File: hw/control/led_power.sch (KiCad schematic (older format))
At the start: 19 parts, among them Q1001 BC807, Q1002 BC817, U801 LM2678T-ADJ

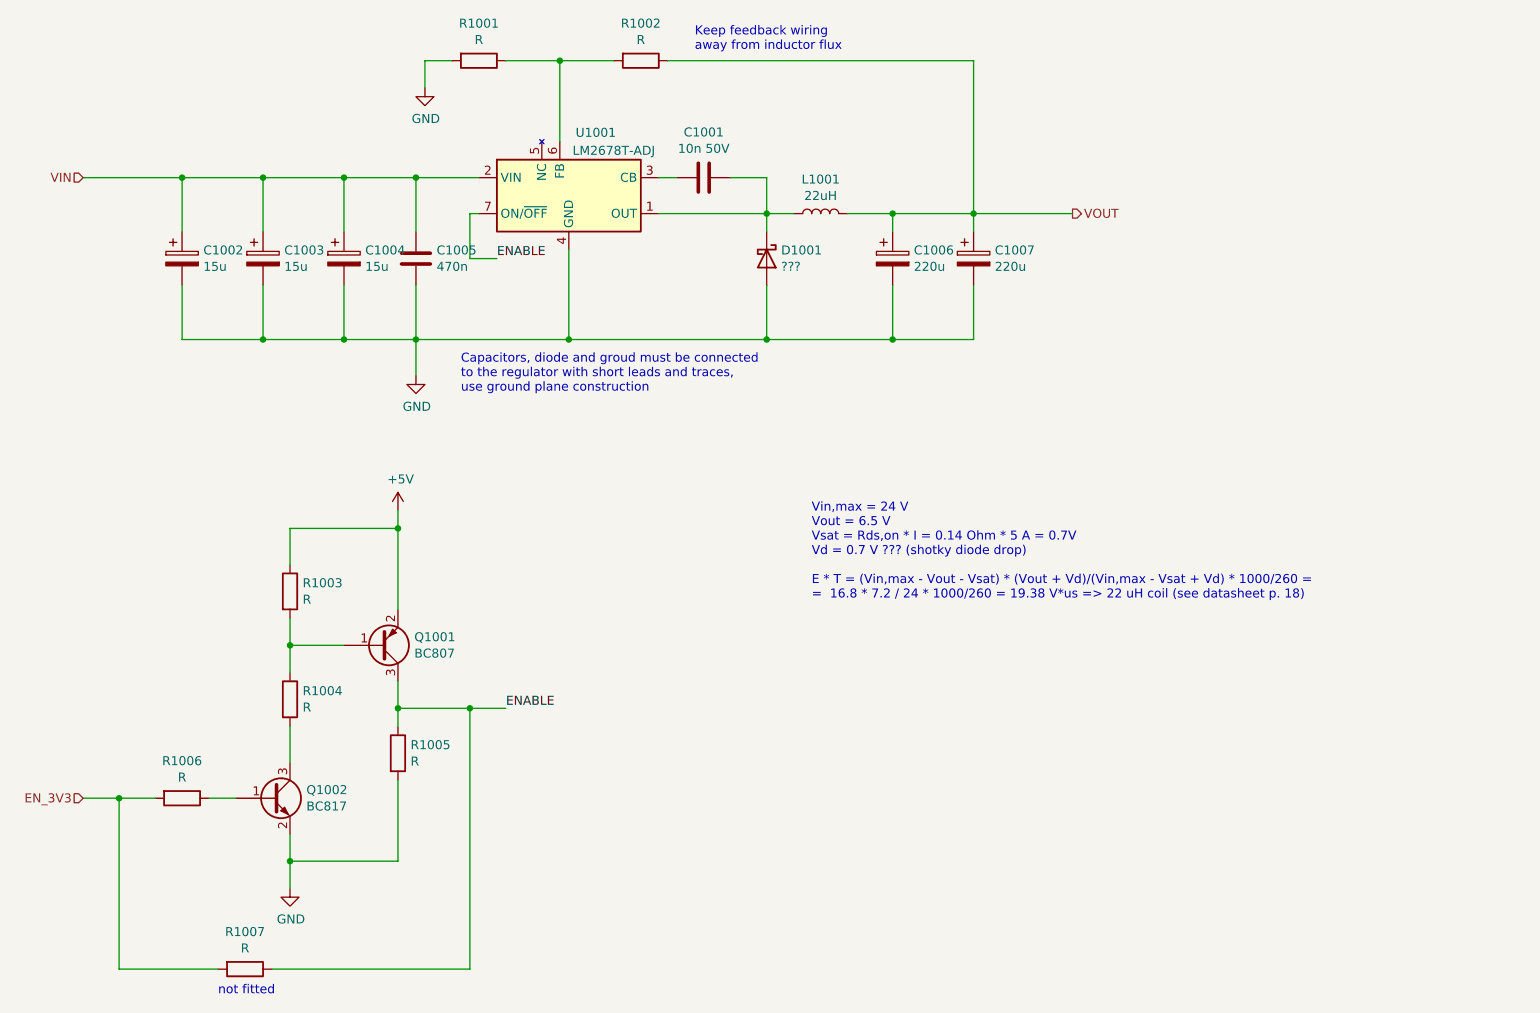
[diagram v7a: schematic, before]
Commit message: [hw] Assign most of the controller footprints
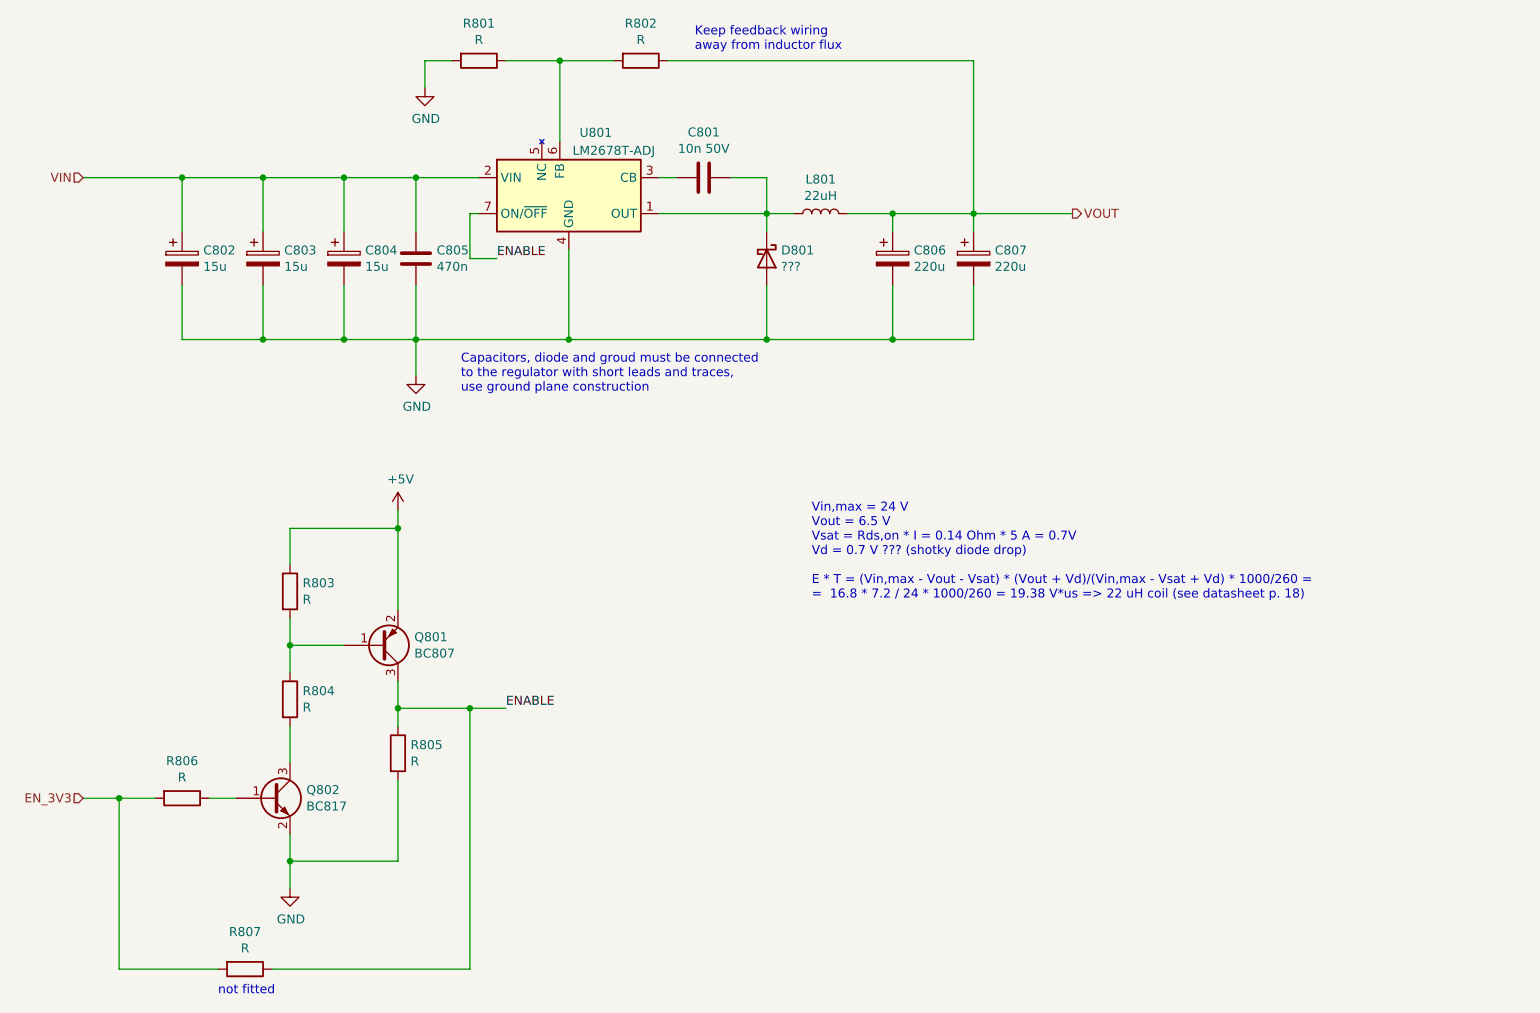
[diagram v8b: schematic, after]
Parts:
- C1005, C801: footprint (none) -> Capacitor_SMD:C_0805_2012Metric_Pad1.18x1.45mm_HandSolder
- D1001: footprint (none) -> Diode_SMD:D_SMC_Handsoldering
- L1001: footprint (none) -> Inductor_THT:L_Toroid_Vertical_L22.4mm_W10.2mm_P7.90mm_Vishay_TJ4
- Q1001, Q1002: footprint (none) -> Package_TO_SOT_SMD:SOT-23_Handsoldering
- R1001, R1002, R1003, R1004, R1005, R1006, R1007: footprint (none) -> Resistor_SMD:R_0805_2012Metric_Pad1.20x1.40mm_HandSolder
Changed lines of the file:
@@
 AR Path="/614AB031/6145ECF0" Ref="U801"  Part="1"
 AR Path="/614AE8DA/6145ECF0" Ref="U1001"  Part="1"
-F 0 "U1001" H 5550 2750 50  0000 C CNN
+F 0 "U801" H 5550 2750 50  0000 C CNN
 F 1 "LM2678T-ADJ" H 5650 2650 50  0000 C CNN
 F 2 "Package_TO_SOT_THT:TO-220-7_P2.54x3.7mm_StaggerOdd_Lead3.8mm_Vertical" H 5450 2150 50  0001 L CIN
@@
 AR Path="/614AB031/6145FC0F" Ref="C801"  Part="1"
 AR Path="/614AE8DA/6145FC0F" Ref="C1001"  Part="1"
-F 0 "C1001" V 5898 2300 50  0000 C CNN
+F 0 "C801" V 5898 2300 50  0000 C CNN
 F 1 "10n 50V" V 5989 2300 50  0000 C CNN
-F 2 "" H 6188 2150 50  0001 C CNN
+F 2 "Capacitor_SMD:C_0805_2012Metric_Pad1.18x1.45mm_HandSolder" H 6188 2150 50  0001 C CNN
 F 3 "~" H 6150 2300 50  0001 C CNN
 	1    6150 2300
@@
 AR Path="/614AB031/61460B18" Ref="#PWR0802"  Part="1"
 AR Path="/614AE8DA/61460B18" Ref="#PWR01002"  Part="1"
-F 0 "#PWR01002" H 4550 3150 50  0001 C CNN
+F 0 "#PWR0802" H 4550 3150 50  0001 C CNN
 F 1 "GND" H 4555 3227 50  0000 C CNN
 F 2 "" H 4550 3400 50  0001 C CNN
@@
 AR Path="/614AE8DA/61461C6E" Ref="D1001"  Part="1"
 AR Path="/614AB031/61461C6E" Ref="D801"  Part="1"
-F 0 "D1001" V 6454 2830 50  0000 L CNN
+F 0 "D801" V 6454 2830 50  0000 L CNN
 F 1 "???" V 6545 2830 50  0000 L CNN
-F 2 "" H 6500 2750 50  0001 C CNN
+F 2 "Diode_SMD:D_SMC_Handsoldering" H 6500 2750 50  0001 C CNN
 F 3 "~" H 6500 2750 50  0001 C CNN
 	1    6500 2750
@@
 AR Path="/614AE8DA/61462D51" Ref="L1001"  Part="1"
 AR Path="/614AB031/61462D51" Ref="L801"  Part="1"
-F 0 "L1001" V 6990 2500 50  0000 C CNN
+F 0 "L801" V 6990 2500 50  0000 C CNN
 F 1 "22uH" V 6899 2500 50  0000 C CNN
-F 2 "" H 6800 2500 50  0001 C CNN
+F 2 "Inductor_THT:L_Toroid_Vertical_L22.4mm_W10.2mm_P7.90mm_Vishay_TJ4" H 6800 2500 50  0001 C CNN
 F 3 "~" H 6800 2500 50  0001 C CNN
 	1    6800 2500
@@
 AR Path="/614AE8DA/61463CC3" Ref="C1006"  Part="1"
 AR Path="/614AB031/61463CC3" Ref="C806"  Part="1"
-F 0 "C1006" H 7318 2796 50  0000 L CNN
+F 0 "C806" H 7318 2796 50  0000 L CNN
 F 1 "220u" H 7318 2705 50  0000 L CNN
 F 2 "" H 7238 2600 50  0001 C CNN
@@
 AR Path="/614AE8DA/6146511A" Ref="C1007"  Part="1"
 AR Path="/614AB031/6146511A" Ref="C807"  Part="1"
-F 0 "C1007" H 7768 2796 50  0000 L CNN
+F 0 "C807" H 7768 2796 50  0000 L CNN
 F 1 "220u" H 7768 2705 50  0000 L CNN
 F 2 "" H 7688 2600 50  0001 C CNN
@@
 AR Path="/614AE8DA/61465477" Ref="C1004"  Part="1"
 AR Path="/614AB031/61465477" Ref="C804"  Part="1"
-F 0 "C1004" H 4268 2796 50  0000 L CNN
+F 0 "C804" H 4268 2796 50  0000 L CNN
 F 1 "15u" H 4268 2705 50  0000 L CNN
 F 2 "" H 4188 2600 50  0001 C CNN
@@
 AR Path="/614AE8DA/614679D1" Ref="C1003"  Part="1"
 AR Path="/614AB031/614679D1" Ref="C803"  Part="1"
-F 0 "C1003" H 3818 2796 50  0000 L CNN
+F 0 "C803" H 3818 2796 50  0000 L CNN
 F 1 "15u" H 3818 2705 50  0000 L CNN
 F 2 "" H 3738 2600 50  0001 C CNN
@@
 AR Path="/614AE8DA/61467CFC" Ref="C1002"  Part="1"
 AR Path="/614AB031/61467CFC" Ref="C802"  Part="1"
-F 0 "C1002" H 3368 2796 50  0000 L CNN
+F 0 "C802" H 3368 2796 50  0000 L CNN
 F 1 "15u" H 3368 2705 50  0000 L CNN
 F 2 "" H 3288 2600 50  0001 C CNN
@@
 AR Path="/614AE8DA/614681BF" Ref="C1005"  Part="1"
 AR Path="/614AB031/614681BF" Ref="C805"  Part="1"
-F 0 "C1005" H 4665 2796 50  0000 L CNN
+F 0 "C805" H 4665 2796 50  0000 L CNN
 F 1 "470n" H 4665 2705 50  0000 L CNN
-F 2 "" H 4588 2600 50  0001 C CNN
+F 2 "Capacitor_SMD:C_0805_2012Metric_Pad1.18x1.45mm_HandSolder" H 4588 2600 50  0001 C CNN
 F 3 "~" H 4550 2750 50  0001 C CNN
 	1    4550 2750
@@
 AR Path="/614AE8DA/6147393D" Ref="R1002"  Part="1"
 AR Path="/614AB031/6147393D" Ref="R802"  Part="1"
-F 0 "R1002" V 5593 1650 50  0000 C CNN
+F 0 "R802" V 5593 1650 50  0000 C CNN
 F 1 "R" V 5684 1650 50  0000 C CNN
-F 2 "" V 5730 1650 50  0001 C CNN
+F 2 "Resistor_SMD:R_0805_2012Metric_Pad1.20x1.40mm_HandSolder" V 5730 1650 50  0001 C CNN
 F 3 "~" H 5800 1650 50  0001 C CNN
 	1    5800 1650
@@
 AR Path="/614AE8DA/61475A47" Ref="R1001"  Part="1"
 AR Path="/614AB031/61475A47" Ref="R801"  Part="1"
-F 0 "R1001" V 4693 1650 50  0000 C CNN
+F 0 "R801" V 4693 1650 50  0000 C CNN
 F 1 "R" V 4784 1650 50  0000 C CNN
-F 2 "" V 4830 1650 50  0001 C CNN
+F 2 "Resistor_SMD:R_0805_2012Metric_Pad1.20x1.40mm_HandSolder" V 4830 1650 50  0001 C CNN
 F 3 "~" H 4900 1650 50  0001 C CNN
 	1    4900 1650
@@
 AR Path="/614AE8DA/61477A40" Ref="#PWR01001"  Part="1"
 AR Path="/614AB031/61477A40" Ref="#PWR0801"  Part="1"
-F 0 "#PWR01001" H 4600 1550 50  0001 C CNN
+F 0 "#PWR0801" H 4600 1550 50  0001 C CNN
 F 1 "GND" H 4605 1627 50  0000 C CNN
 F 2 "" H 4600 1800 50  0001 C CNN
@@
 AR Path="/614AE8DA/6147DB7E" Ref="R1006"  Part="1"
 AR Path="/614AB031/6147DB7E" Ref="R806"  Part="1"
-F 0 "R1006" V 3043 5750 50  0000 C CNN
+F 0 "R806" V 3043 5750 50  0000 C CNN
 F 1 "R" V 3134 5750 50  0000 C CNN
-F 2 "" V 3180 5750 50  0001 C CNN
+F 2 "Resistor_SMD:R_0805_2012Metric_Pad1.20x1.40mm_HandSolder" V 3180 5750 50  0001 C CNN
 F 3 "~" H 3250 5750 50  0001 C CNN
 	1    3250 5750
@@
 AR Path="/614AE8DA/6147EFCD" Ref="Q1002"  Part="1"
 AR Path="/614AB031/6147EFCD" Ref="Q802"  Part="1"
-F 0 "Q1002" H 3941 5796 50  0000 L CNN
+F 0 "Q802" H 3941 5796 50  0000 L CNN
 F 1 "BC817" H 3941 5705 50  0000 L CNN
-F 2 "" H 3950 5850 50  0001 C CNN
+F 2 "Package_TO_SOT_SMD:SOT-23_Handsoldering" H 3950 5850 50  0001 C CNN
 F 3 "~" H 3750 5750 50  0001 C CNN
 	1    3750 5750
@@
 AR Path="/614AE8DA/61480A0D" Ref="Q1001"  Part="1"
 AR Path="/614AB031/61480A0D" Ref="Q801"  Part="1"
-F 0 "Q1001" H 4541 4854 50  0000 L CNN
+F 0 "Q801" H 4541 4854 50  0000 L CNN
 F 1 "BC807" H 4541 4945 50  0000 L CNN
-F 2 "" H 4550 5000 50  0001 C CNN
+F 2 "Package_TO_SOT_SMD:SOT-23_Handsoldering" H 4550 5000 50  0001 C CNN
 F 3 "~" H 4350 4900 50  0001 C CNN
 	1    4350 4900
@@
 AR Path="/614AE8DA/6148128F" Ref="R1004"  Part="1"
 AR Path="/614AB031/6148128F" Ref="R804"  Part="1"
-F 0 "R1004" H 3920 5246 50  0000 L CNN
+F 0 "R804" H 3920 5246 50  0000 L CNN
 F 1 "R" H 3920 5155 50  0000 L CNN
-F 2 "" V 3780 5200 50  0001 C CNN
+F 2 "Resistor_SMD:R_0805_2012Metric_Pad1.20x1.40mm_HandSolder" V 3780 5200 50  0001 C CNN
 F 3 "~" H 3850 5200 50  0001 C CNN
 	1    3850 5200
@@
 AR Path="/614AE8DA/614817B0" Ref="R1003"  Part="1"
 AR Path="/614AB031/614817B0" Ref="R803"  Part="1"
-F 0 "R1003" H 3920 4646 50  0000 L CNN
+F 0 "R803" H 3920 4646 50  0000 L CNN
 F 1 "R" H 3920 4555 50  0000 L CNN
-F 2 "" V 3780 4600 50  0001 C CNN
+F 2 "Resistor_SMD:R_0805_2012Metric_Pad1.20x1.40mm_HandSolder" V 3780 4600 50  0001 C CNN
 F 3 "~" H 3850 4600 50  0001 C CNN
 	1    3850 4600
@@
 AR Path="/614AE8DA/61483286" Ref="#PWR01004"  Part="1"
 AR Path="/614AB031/61483286" Ref="#PWR0804"  Part="1"
-F 0 "#PWR01004" H 3850 6000 50  0001 C CNN
+F 0 "#PWR0804" H 3850 6000 50  0001 C CNN
 F 1 "GND" H 3855 6077 50  0000 C CNN
 F 2 "" H 3850 6250 50  0001 C CNN
@@
 AR Path="/614AE8DA/61486663" Ref="#PWR01003"  Part="1"
 AR Path="/614AB031/61486663" Ref="#PWR0803"  Part="1"
-F 0 "#PWR01003" H 4450 4000 50  0001 C CNN
+F 0 "#PWR0803" H 4450 4000 50  0001 C CNN
 F 1 "+5V" H 4465 4323 50  0000 C CNN
 F 2 "" H 4450 4150 50  0001 C CNN
@@
 AR Path="/614AE8DA/6148D73D" Ref="R1005"  Part="1"
 AR Path="/614AB031/6148D73D" Ref="R805"  Part="1"
-F 0 "R1005" H 4520 5546 50  0000 L CNN
+F 0 "R805" H 4520 5546 50  0000 L CNN
 F 1 "R" H 4520 5455 50  0000 L CNN
-F 2 "" V 4380 5500 50  0001 C CNN
+F 2 "Resistor_SMD:R_0805_2012Metric_Pad1.20x1.40mm_HandSolder" V 4380 5500 50  0001 C CNN
 F 3 "~" H 4450 5500 50  0001 C CNN
 	1    4450 5500
@@
 AR Path="/614AE8DA/614CC1BE" Ref="R1007"  Part="1"
 AR Path="/614AB031/614CC1BE" Ref="R807"  Part="1"
-F 0 "R1007" V 3393 6700 50  0000 C CNN
+F 0 "R807" V 3393 6700 50  0000 C CNN
 F 1 "R" V 3484 6700 50  0000 C CNN
-F 2 "" V 3530 6700 50  0001 C CNN
+F 2 "Resistor_SMD:R_0805_2012Metric_Pad1.20x1.40mm_HandSolder" V 3530 6700 50  0001 C CNN
 F 3 "~" H 3600 6700 50  0001 C CNN
 	1    3600 6700
